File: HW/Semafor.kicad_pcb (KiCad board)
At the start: 2 copper layers, 148.8 x 160.7 mm, 97 parts, among them J1 USB_C_Receptacle_USB2.0, J2 USB_plug, J3 Conn_01x03_Male, M1 Motor_DC, Q1 Q_NMOS_GSD, Q2 Q_PMOS_GSD, Q3 Q_NMOS_GSD, Q4 Q_NMOS_GSD, Q5 Q_Photo_NPN, SW6 SW_SPDT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

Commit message: start drawing small version of Module, draw stepup as per datasheet
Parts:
- removed D15: Green, LED_SMD:LED_0603_1608Metric
- removed D23: D_Schottky, Diode_SMD:D_SOD-123
- removed D25: SD05_SOD323, Diode_SMD:D_SOD-323
- removed J2: USB_plug, Library:USB_plug
- removed R11: 10k, Resistor_SMD:R_0603_1608Metric
- BT1: moved to F.Cu
- BTN1_ENTER1: footprint Library:Cap_btn_5x5 -> Library:Cap_btn_2,5x2,5
- BTN2_UP1, BTN3_DOWN1, BTN4_RIGHT1, BTN5_LEFT1: footprint Library:Cap_btn_2x2 -> Library:Cap_btn_1,6x1,6
- moved C25 337.6 mm to (201.5, 45.5)
- moved D22 337.6 mm to (205.4, 45.5)
- moved M1 337.6 mm to (196.7, 44.4)
- moved Q4 337.6 mm to (196.6, 52.1)
- moved R15 337.6 mm to (196.6, 56.4)
- moved R27 308.4 mm to (142.0, 38.1), turned to 0 degrees
- moved D12 307.1 mm to (77.5, 61.0)
- moved D11 307.1 mm to (61.0, 77.4)
- moved C12 306.9 mm to (80.8, 63.2)
- moved R3 306.9 mm to (52.9, 168.8), turned to 0 degrees
- moved C19 306.7 mm to (65.0, 77.7)
- moved C10 305.9 mm to (113.5, 155.1)
- moved D14 305.9 mm to (118.8, 160.4)
- moved C1 305.9 mm to (107.6, 157.1)
- moved D13 305.9 mm to (120.6, 160.4)
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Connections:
- net FOTOTRANZISTOR renamed PHOTOTRANZISTOR
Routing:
- net PWR_LED: track 476.9 -> 0.00 mm, vias 2 -> 0
- net GND: track 363.6 -> 104.3 mm, vias 19 -> 1
- net 3V3_SWITCHED: track 250.9 -> 24.6 mm, vias 3 -> 0
- net +3V3: track 210.4 -> 23.0 mm, vias 3 -> 0
- net RX_LoRa: track 141.5 -> 0.00 mm, vias 1 -> 0
- net TX_LoRa: track 135.1 -> 0.00 mm, vias 1 -> 0
- net +5V: track 126.7 -> 14.7 mm, vias 2 -> 0
- net PHOTOTRANZISTOR: track 91.7 -> 2.54 mm, vias 3 -> 0
- net MOTOR: track 84.0 -> 4.74 mm, vias 2 -> 0
- net DATA_LED: track 81.6 -> 4.63 mm, vias 1 -> 0
- net PIEZO: track 76.9 -> 3.54 mm, vias 2 -> 0
- net SCL: track 59.3 -> 2.50 mm, vias 2 -> 0
- net SDA: track 58.7 -> 2.53 mm, vias 4 -> 0
- net D+: track 67.0 -> 11.4 mm
- net D-: track 67.4 -> 13.3 mm, vias 2 -> 0
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- removed copper zone on B.Cu, net GND
- removed copper zone on F.Cu, net GND
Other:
- board size 148.8 x 160.7 mm -> 100 x 100 mm
- board text added: "Tlusčí dráhy"
- board text added: "Univerzální modul pro podporu týmových her 1.0 by Renata Zemanová"
- board text removed: "Semafor 0.0 by Renata Zemanová"
- board text removed: "step up"

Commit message: continue routing
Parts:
- BT1: moved to B.Cu
- C1, C10, D13, D14, R6, R8, U2: moved to F.Cu
- moved D18 61.7 mm to (96.5, 136.9), turned to 75 degrees
- moved R8 60.1 mm to (72.3, 110.8), turned to 90 degrees
- moved D13 59.9 mm to (73.1, 124.0), turned to 0 degrees
- moved C1 59.7 mm to (69.8, 111.0), turned to 90 degrees
- moved C10 59.6 mm to (67.8, 116.9), turned to 90 degrees
- moved D14 59.6 mm to (73.1, 122.2), turned to 0 degrees
- moved R6 59.4 mm to (75.5, 121.3), turned to -90 degrees
- moved U2 59.4 mm to (71.7, 117.2), turned to -90 degrees
- moved D24 58.5 mm to (94.2, 137.0), turned to -105 degrees
- moved D19 54.1 mm to (91.2, 136.3), turned to 165 degrees
- moved R2 52.4 mm to (91.3, 138.0), turned to -15 degrees
- moved D20 49.8 mm to (87.9, 135.4), turned to -15 degrees
- moved R3 46.8 mm to (87.3, 137.1), turned to 165 degrees
- moved J1 41.6 mm to (87.9, 143.8), turned to 165 degrees
- moved D16 33.1 mm to (57.7, 102.5)
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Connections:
- D1 pad 4: DATA_LED -> DATA_LED_OUT
- Q1 pad 3: DATA_LED -> DATA_LED_OUT
- R4 pad 2: DATA_LED -> DATA_LED_OUT
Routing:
- net unconnected-(U1-Pad10): track 25.2 -> 44.5 mm, vias 0 -> 2
- net PWR_LED: track 0.00 -> 11.6 mm
- net +3V3: track 23.0 -> 27.1 mm
- net Net-(Q2-Pad1): track 1.33 -> 5.24 mm, vias 0 -> 2
- net U_BAT_ADC: track 1.33 -> 4.09 mm
- net GND: track 104.3 -> 101.8 mm
- net PHOTOTRANZISTOR: track 2.54 -> 4.97 mm
- net RX_LoRa: track 0.00 -> 2.43 mm, vias 0 -> 1
- net TX_LoRa: track 0.00 -> 2.32 mm, vias 0 -> 1
- net 3V3_SWITCHED: track 24.6 -> 26.5 mm
- net DATA_LED_OUT: track 0.00 -> 1.80 mm
- net MOTOR: track 4.74 -> 4.75 mm, vias 0 -> 1
- net PIEZO: track 3.54 -> 3.55 mm, vias 0 -> 1

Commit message: done routing of version 1.0
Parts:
- BTN1_ENTER1: footprint Library:Cap_btn_2,5x2,5 -> Library:Cap_btn_2x2
- C13, C14, C3, C4, D17, L1, R10, R13, R16, R17, R18, R19, R20, R21, R22, R23, R9, U3, U5: moved to F.Cu
- moved BTN1_ENTER1 409.9 mm to (100.0, 100.0)
- moved D22 101.9 mm to (105.4, 65.2)
- moved R15 101.8 mm to (95.3, 66.3), turned to 90 degrees
- moved Q4 99.4 mm to (98.2, 66.1), turned to 0 degrees
- moved M1 96.5 mm to (102.1, 63.6)
- moved C25 95.8 mm to (107.5, 64.3)
- moved D17 87.2 mm to (75.0, 119.6), turned to 90 degrees
- moved L1 84.3 mm to (73.7, 114.6), turned to 0 degrees
- moved C14 83.7 mm to (78.3, 118.3), turned to 0 degrees
- moved R10 82.1 mm to (81.0, 118.8), turned to -90 degrees
- moved C13 81.4 mm to (77.1, 113.9), turned to -90 degrees
- moved R9 81.0 mm to (82.6, 118.8), turned to 90 degrees
- moved U3 80.1 mm to (80.0, 114.9), turned to 90 degrees
- moved R13 78.1 mm to (79.9, 111.6), turned to 0 degrees
- moved R17 69.0 mm to (119.4, 128.3), turned to 90 degrees
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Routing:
- net PWR_LED: track 11.6 -> 390.9 mm, vias 0 -> 13
- net GND: track 101.8 -> 256.5 mm, vias 1 -> 30
- net 3V3_SWITCHED: track 26.5 -> 173.5 mm, vias 0 -> 1
- net +3V3: track 27.1 -> 114.9 mm, vias 0 -> 4
- net SCL: track 2.50 -> 75.3 mm, vias 0 -> 1
- net SDA: track 2.53 -> 73.5 mm, vias 0 -> 1
- net RX_LoRa: track 2.43 -> 72.1 mm, vias 1 -> 2
- net TX_LoRa: track 2.32 -> 69.9 mm, vias 1 -> 2
- net D+: track 11.4 -> 78.2 mm
- net D-: track 13.3 -> 79.0 mm
- net DATA_LED_SIDE: track 2.43 -> 47.7 mm, vias 1 -> 2
- net Net-(BTN5_LEFT1-Pad1): track 22.5 -> 58.0 mm, vias 0 -> 2
- net DATA_LED_OUT: track 1.80 -> 36.4 mm, vias 0 -> 5
- net Net-(BTN2_UP1-Pad1): track 17.2 -> 50.4 mm
- net Net-(BTN4_RIGHT1-Pad1): track 44.5 -> 15.9 mm
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- added copper zone on B.Cu, net GND
- added copper zone on F.Cu, net GND
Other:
- board text removed: "Tlusčí dráhy"

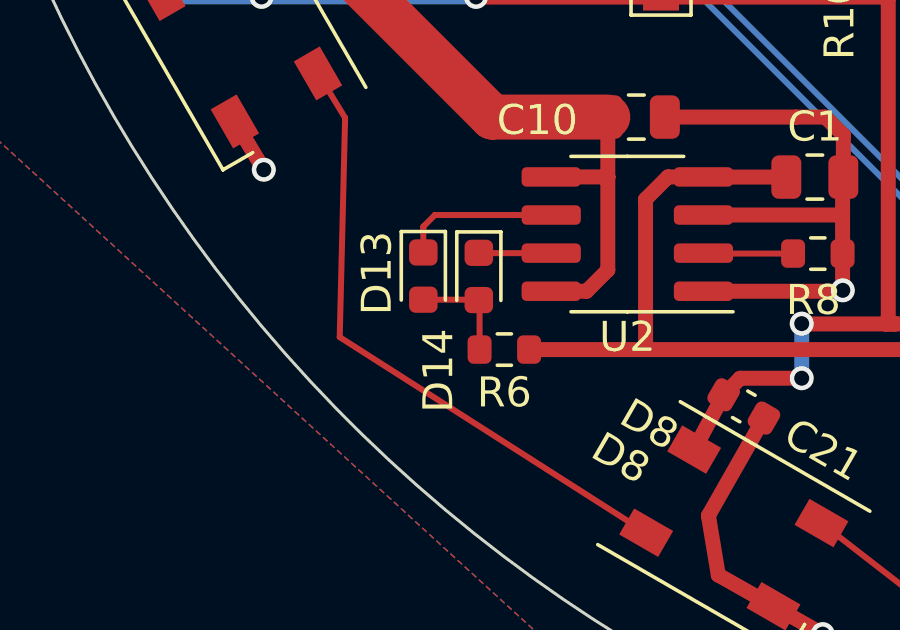
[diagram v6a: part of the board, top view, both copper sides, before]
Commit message: charging LEDs place to PCB bottom
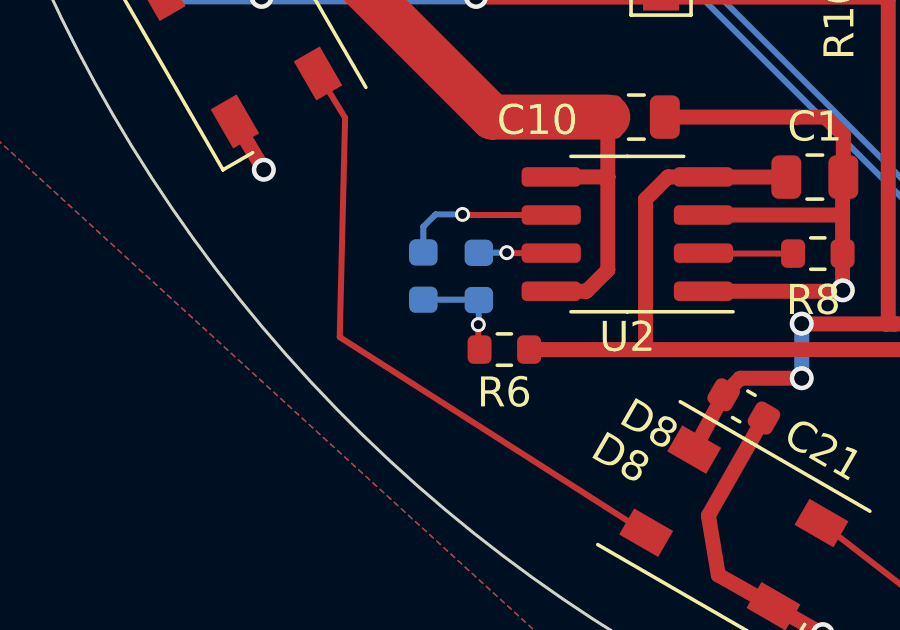
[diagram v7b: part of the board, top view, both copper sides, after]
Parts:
- D13, D14: moved to B.Cu
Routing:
- net Net-(D13-Pad1): track 5.28 -> 5.30 mm, vias 0 -> 1
- net Net-(D13-Pad2): track 3.52 -> 3.53 mm, vias 0 -> 1
- net Net-(D14-Pad1): vias 0 -> 1

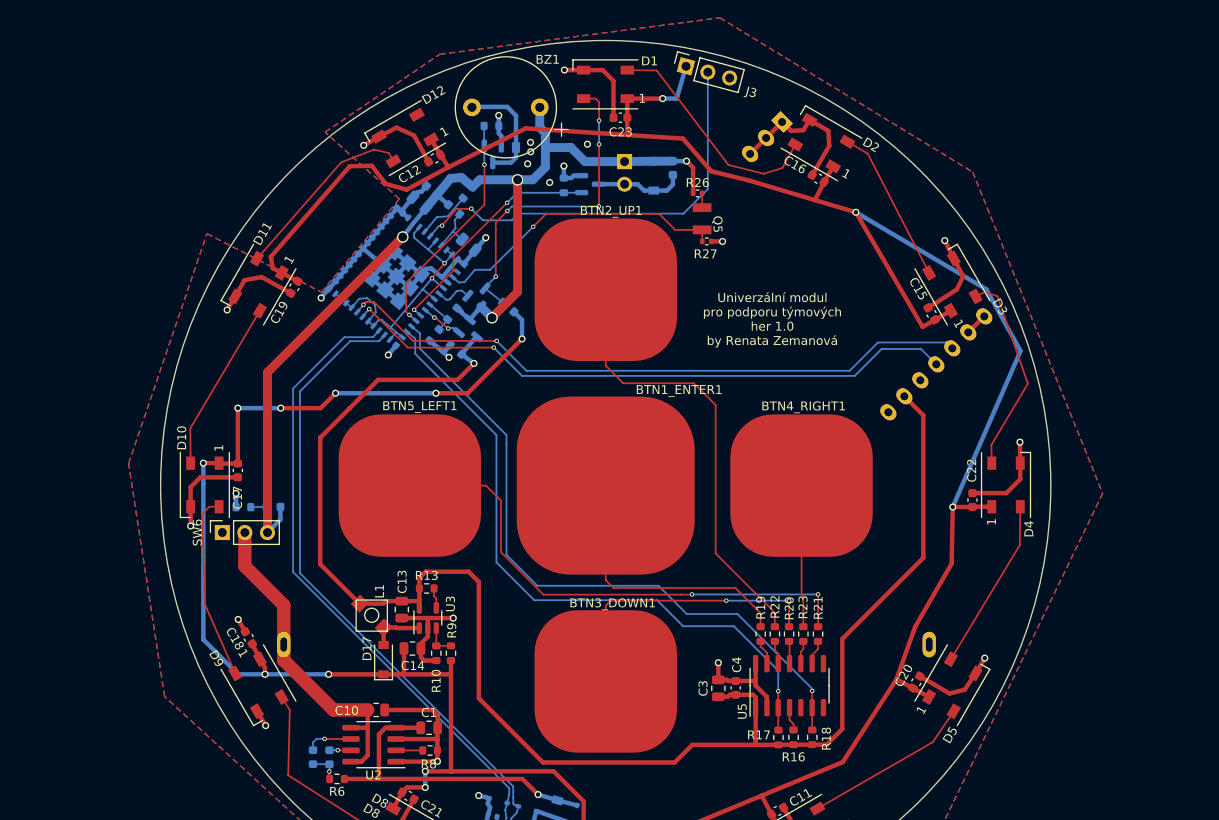
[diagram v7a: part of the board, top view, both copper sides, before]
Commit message: repair mistakes and preparing for 2 PCBs (sandwich)
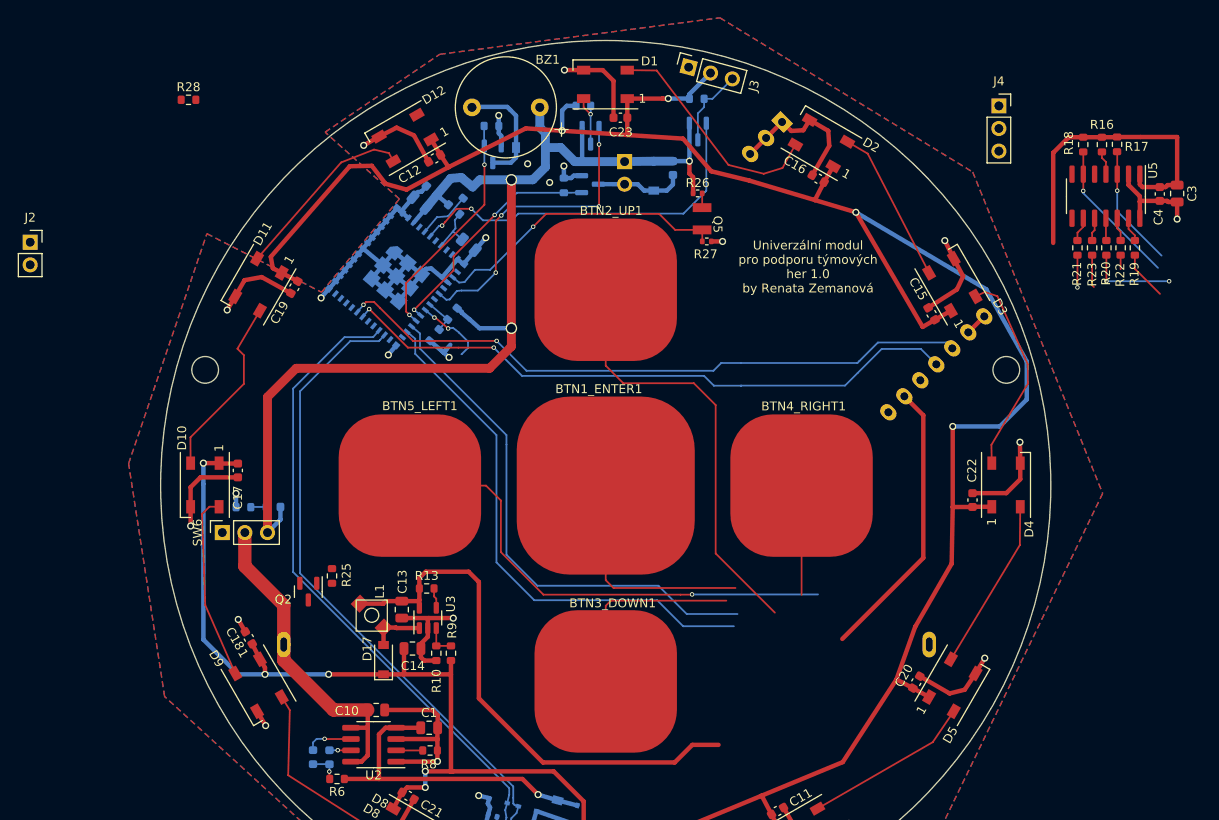
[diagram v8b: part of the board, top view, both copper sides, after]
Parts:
- added J2: Conn_01x02_Female, Connector_PinSocket_2.54mm:PinSocket_1x02_P2.54mm_Vertical, F.Cu at (35.3, 72.7)
- added J4: Conn_01x03_Male, Connector_PinSocket_2.54mm:PinSocket_1x03_P2.54mm_Vertical, F.Cu at (144.2, 57.3)
- added Q6: Q_NMOS_GSD, Package_TO_SOT_SMD:SOT-23, B.Cu at (110.3, 60.2)
- added R11: 10k, Resistor_SMD:R_0603_1608Metric, B.Cu at (110.2, 56.5)
- added R28: 180R, Resistor_SMD:R_0603_1608Metric, F.Cu at (53.1, 56.7)
- Q2, R25: moved to F.Cu
- moved R17 76.7 mm to (157.4, 61.7), turned to -90 degrees
- moved C3 75.8 mm to (164.2, 67.2), turned to -90 degrees
- moved R16 75.1 mm to (155.7, 61.7), turned to -90 degrees
- moved R18 73.2 mm to (153.6, 61.7), turned to -90 degrees
- moved C4 73.1 mm to (162.2, 67.2), turned to -90 degrees
- moved U5 65.5 mm to (156.2, 67.5), turned to -90 degrees
- moved R19 60.4 mm to (159.4, 73.3), turned to -90 degrees
- moved R22 58.2 mm to (157.8, 73.3), turned to -90 degrees
- moved R20 56.1 mm to (156.2, 73.3), turned to -90 degrees
- moved R23 54.2 mm to (154.6, 73.3), turned to -90 degrees
- moved R21 52.3 mm to (153.0, 73.3), turned to 90 degrees
- moved Q2 34.5 mm to (66.6, 111.9), turned to -90 degrees
- moved R25 29.0 mm to (69.2, 110.2), turned to 90 degrees
- moved R4 24.1 mm to (97.5, 57.3), turned to 0 degrees
- moved Q1 21.8 mm to (98.3, 60.7), turned to -90 degrees
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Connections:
- J3 pad 1: PWR_LED -> GND
- J3 pad 2: DATA_LED_SIDE -> PWR_LED
- J3 pad 3: GND -> Net-(J3-Pad3)
- R25 pad 1: 3V3_SWITCHED -> Net-(Q2-Pad1)
- R25 pad 2: GND -> +3V3
- U1 pad 10: unconnected-(U1-Pad10) -> (no net)
- U1 pad 15: unconnected-(U1-Pad10) -> (no net)
- U1 pad 17: unconnected-(U1-Pad10) -> (no net)
- U1 pad 24: unconnected-(U1-Pad10) -> (no net)
- U1 pad 25: unconnected-(U1-Pad10) -> (no net)
- U1 pad 28: unconnected-(U1-Pad10) -> (no net)
- U1 pad 29: unconnected-(U1-Pad10) -> (no net)
- U1 pad 32: unconnected-(U1-Pad10) -> (no net)
- U1 pad 33: unconnected-(U1-Pad10) -> (no net)
- U1 pad 34: unconnected-(U1-Pad10) -> (no net)
- U1 pad 35: unconnected-(U1-Pad10) -> (no net)
- U1 pad 4: unconnected-(U1-Pad10) -> (no net)
- U1 pad 7: unconnected-(U1-Pad10) -> (no net)
- U1 pad 9: unconnected-(U1-Pad10) -> (no net)
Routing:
- net 3V3_SWITCHED: track 173.5 -> 129.1 mm, vias 1 -> 0
- net unconnected-(U1-Pad10): track 36.2 -> 0.00 mm, vias 2 -> 0
- net PWR_LED: track 390.9 -> 356.8 mm, vias 13 -> 9
- net DATA_LED: track 4.16 -> 34.8 mm, vias 0 -> 4
- net DATA_LED_OUT: track 36.4 -> 6.38 mm, vias 5 -> 1
- net +3V3: track 114.9 -> 130.0 mm, vias 4 -> 3
- net Net-(J3-Pad3): track 0.00 -> 9.00 mm
- net DATA_LED_SIDE: track 47.7 -> 41.9 mm
- net Net-(Q2-Pad1): track 4.73 -> 7.89 mm
- net Net-(D10-Pad2): track 19.3 -> 20.6 mm
- net TX_LoRa: track 69.9 -> 70.8 mm
- net GND: vias 30 -> 27
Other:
- outline, holes or cut-outs redrawn
